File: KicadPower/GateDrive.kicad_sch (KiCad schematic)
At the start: 23 parts, among them U13 1EDN7116UXTSA1, U15 1EDN7116UXTSA1, U5 LDK220C, U9 LDK220C-R

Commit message: minor changes
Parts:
- renumbered C192 to C191, C199 to C198, C202 to C201, C204 to C203, D8 to D10, D11 to D12, FB5 to FB4, R39 to R40, R42 to R43, R44 to R46, R53 to R55, R58 to R57, U13 to U12, U15 to U16, U5 to U7, U9 to U8
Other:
- moved on the sheet: C185, C190, C191, C196, C198, C201, C203, D10, D12, D3, D6, FB4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

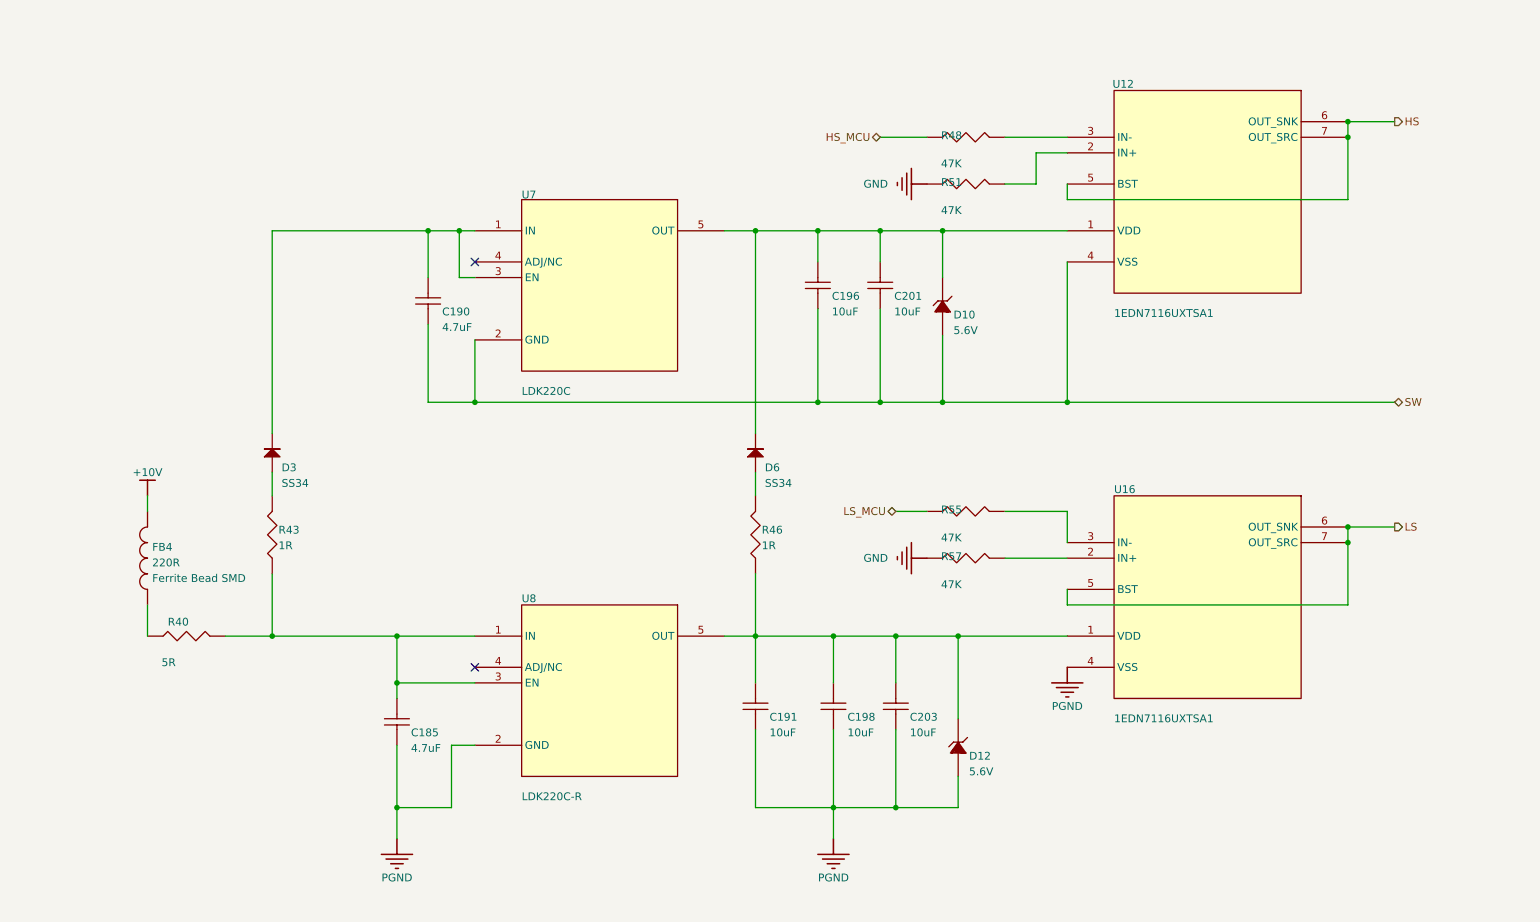
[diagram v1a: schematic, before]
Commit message: new G serie of Driver modifed and finished
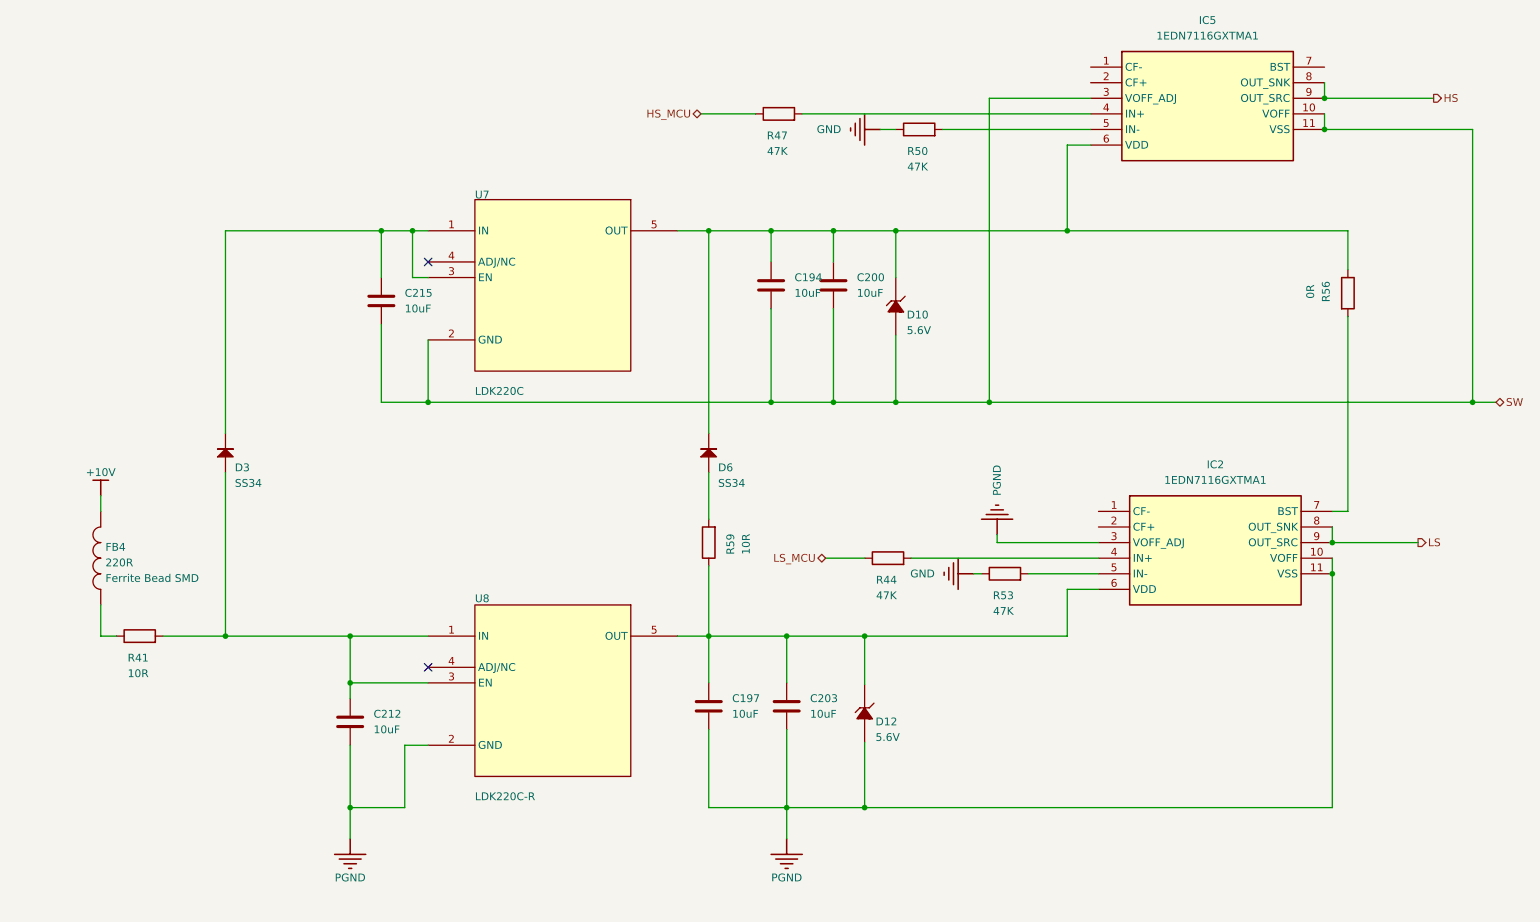
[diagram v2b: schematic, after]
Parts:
- removed C185, C190, C191, C196, C198, C201, C203: Cap SMD, CAPC2012X135N, symbol RezaLIB:U_GateDrive_1_Cap SMD_RezaLIB.IntLib
- removed R40, R48, R51, R55, R57: Res SMD, RESC1608X55N, symbol RezaLIB:U_GateDrive_0_Res SMD_RezaLIB.IntLib
- removed R43, R46: Res SMD, RESC1608X55N, symbol RezaLIB:U_GateDrive_1_Res SMD_RezaLIB.IntLib
- removed U12, U16: 1EDN7116UXTSA1, PG-TSNP-7-11_INF, symbol RezaLIB:U_GateDrive_0_1EDN7116UXTSA1_RezaLIB.IntLib
- added C194, C197, C200, C203, C212, C215: 10uF, Capacitor_SMD:C_0603_1608Metric, symbol Device:C
- added IC2, IC5: 1EDN7116GXTMA1, 1EDN7116GXTMA1, symbol 1EDN7116GXTMA1:1EDN7116GXTMA1
- added R41, R59: 10R, Resistor_SMD:R_0603_1608Metric_Pad0.98x0.95mm_HandSolder, symbol Device:R
- added R44, R47, R50, R53: 47K, Resistor_SMD:R_0603_1608Metric_Pad0.98x0.95mm_HandSolder, symbol Device:R
- added R56: 0R, Resistor_SMD:R_0603_1608Metric_Pad0.98x0.95mm_HandSolder, symbol Device:R
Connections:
- net GND: now also R50.1, R53.1
- net HS: now also IC5.8 (OUT_SNK), IC5.9 (OUT_SRC)
- net HS_MCU: now also R47.1
- net LS: now also IC2.8 (OUT_SNK), IC2.9 (OUT_SRC)
- net LS_MCU: now also R44.1
- net PGND: now also C197.2, C203.2, C212.2, IC2.10 (VOFF), IC2.11 (VSS), IC2.3 (VOFF_ADJ)
- net SW: now also C194.2, C200.2, C215.2, IC5.10 (VOFF), IC5.11 (VSS), IC5.3 (VOFF_ADJ)
- net at U8.1 (IN), U8.3 (EN): now also D3.A (1), C212.1, R41.2
- net at D12.1, U8.5 (OUT): now also C197.1, C203.1, IC2.6 (VDD), R59.1
- net at FB4.1: now also R41.1
- net at D10.1, D6.K (2), U7.5 (OUT): now also C194.1, C200.1, IC5.6 (VDD), R56.1
- net at D6.A (1): now also R59.2
- net at D3.K (2), U7.1 (IN), U7.3 (EN): now also C215.1
- new net: IC2.5 (IN-), R53.2
- new net: IC2.4 (IN+), R44.2
- new net: IC2.7 (BST), R56.2
- new net: IC5.4 (IN+), R47.2
- new net: IC5.5 (IN-), R50.2
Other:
- moved on the sheet: D10, D12, D3, D6, FB4, U7, U8
